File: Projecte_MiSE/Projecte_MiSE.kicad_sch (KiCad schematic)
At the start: 30 parts, among them J1 conn_DFrobot, U1 LMV324

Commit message: components add
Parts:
- removed C?: 100n, Capacitor_SMD:C_0805_2012Metric, symbol Device:C
- removed J?: ESP01_WiFi_mod, Connector_PinSocket_2.54mm:PinSocket_2x04_P2.54mm_Vertical, symbol Connector_Generic:Conn_02x04_Odd_Even
- removed J?: Conn_RX_TP, Connector_PinHeader_2.00mm:PinHeader_1x01_P2.00mm_Vertical, symbol Connector:Conn_01x01_Pin
- removed J?: Conn_TX_TP, Connector_PinHeader_2.00mm:PinHeader_1x01_P2.00mm_Vertical, symbol Connector:Conn_01x01_Pin
- removed J?: Conn_01x03, symbol Connector_Generic:Conn_01x03
- removed J?: Conn_01x05, symbol Connector_Generic:Conn_01x05
- removed R?: R, symbol Device:R
- added C? (x6): C, symbol Device:C
- added C_RXD: C_TXD, symbol Connector:Conn_01x02_Pin
- added J?: Conn_01x03_Pin, symbol Connector:Conn_01x03_Pin
- added J?: ESP01, symbol Connector_Generic:Conn_02x04_Odd_Even
- added J?: URM10, symbol Connector:Conn_01x05_Pin
- added R? (x3): R, symbol Device:R
- J1: value conn_DFrobot -> C_DFrobot
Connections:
- net +3.3V: now also LCD?.1 (VDD), C?.1, C?.1, C?.1, J?.2 (Pin_2), R?.1, R?.1, R?.1; no longer J1.1 (Pin_1), J1.2 (Pin_2)
- net GND: now also LCD?.2 (VSS), LCD?.6 (A), LCD?.7 (K), C?.2, C?.2, C?.2, C?.2, C?.2, C?.2, J?.3 (Pin_3), J?.5 (Pin_5), J?.7 (Pin_7)
- net GPIOD: now also IC?.36 (P3.6/OA3-)
- net GPIOL: now also IC?.44 (P3.3/OA2+)
- net GPIOR: now also IC?.45 (P3.2/OA2-)
- net GPIOU: now also IC?.35 (P3.7/OA3+)
- net JSEL: now also IC?.37 (P3.5/OA3O); no longer IC?.44 (P3.3/OA2+)
- net at IC?.12 (P4.7/UCB1SOMI/UCB1SCL), J1.9 (Pin_9): now also LCD?.4 (SCL), R?.2
- net at IC?.13 (P4.6/UCB1SIMO/UCB1SDA), J1.11 (Pin_11): now also LCD?.3 (SDA), R?.2
- net at IC?.14 (P4.5/UCB1CLK): now also LCD?.5 (RST)
- net EN: now reaches IC?.17 (P6.5/TB3.6)
- net EN: now also J?.6 (Pin_6), R?.2
- net P12: now reaches IC?.18 (P6.4/TB3.5)
- net P12: now also J1.12 (Pin_12)
- net P8: now reaches IC?.19 (P6.3/TB3.4)
- net P8: now also J1.10 (Pin_10)
- net P2: now reaches IC?.20 (P6.2/TB3.3)
- net P2: now also J1.8 (Pin_8)
- net P1: now reaches IC?.21 (P6.1/TB3.2)
- net P1: now also J1.6 (Pin_6)
- net P0: now reaches IC?.22 (P6.0/TB3.1)
- net P0: now also J1.4 (Pin_4)
- net TXD: now reaches IC?.23 (P4.3/UCA1TXD/UCA1SIMO/~{UCA1TXD})
- net TXD: now also C_RXD.1 (Pin_1), J?.8 (Pin_8)
- net RXD: now reaches IC?.24 (P4.2/UCA1RXD/UCA1SOMI/~{UCA1RXD})
- net RXD: now also C_RXD.2 (Pin_2), J?.1 (Pin_1)
- net trg: now reaches IC?.27 (P2.3/TB1TRG)
- net trg: now also J?.3 (Pin_3)
- net at IC?.29 (P2.1/TB1.2/COMP1.O): now also J?.2 (Pin_2)
- net MOSI: now reaches IC?.31 (P1.7/UCA0TXD/UCA0SIMO/TB0.2/TDO/OA1+/A7/VREF+)
- net MOSI: now also J1.7 (Pin_7)
- net MISO: now reaches IC?.32 (P1.6/UCA0RXD/UCA0SOMI/TB0.1/TDI/TCLK/OA1-/A6)
- net MISO: now also J1.5 (Pin_5)
- net SCLK: now reaches IC?.33 (P1.5/UCA0CLK/TMS/OA1O/A5)
- net SCLK: now also J1.3 (Pin_3)
- net at IC?.4 (TEST/SBWTCK): now also J?.2 (Pin_2)
- net at C?.1, IC?.5 (~{RST}/NMI/SBWTDIO), R?.2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: now also J?.1 (Pin_1)
- new net: C?.1, J1.1 (Pin_1)
- new net: C?.1, J?.1 (Pin_1)
- new net: C?.1, J1.2 (Pin_2)
- no-connect marks 14 -> 29
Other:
- moved on the sheet: C?, IC?, J1, LCD?, R1, R2, R?, RV1, RV?, S1, SW?, U1A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

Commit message: LAYOUT_RULES
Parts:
- C1, C10, C11, C2, C3, C4, C5, C6, C7, C8, C9: renamed from C?; footprint (none) -> Capacitor_SMD:C_0805_2012Metric
- C_RXD1: renamed from C_RXD; footprint (none) -> Connector_PinHeader_2.54mm:PinHeader_1x02_P2.54mm_Vertical
- IC1: renamed from IC?; footprint MiSE:QFP50P900X900X160-48N -> Package_QFP:LQFP-48_7x7mm_P0.5mm
- J2: renamed from J?; footprint (none) -> Connector_PinHeader_2.54mm:PinHeader_1x03_P2.54mm_Vertical
- J3: renamed from J?; footprint (none) -> Connector_PinSocket_2.54mm:PinSocket_2x04_P2.54mm_Vertical
- J4: renamed from J?; footprint (none) -> Connector_PinSocket_2.54mm:PinSocket_1x05_P2.54mm_Vertical
- LCD1: renamed from LCD?; footprint MiSE:LCD_2x16_I2C(Midas) -> Connector_PinSocket_2.54mm:PinSocket_2x04_P2.54mm_Vertical
- R1: footprint (none) -> Resistor_SMD:R_0805_2012Metric
- R10, R11, R12, R3, R4, R5, R7, R8, R9: renamed from R?; footprint (none) -> Resistor_SMD:R_0805_2012Metric
- S1: footprint THB001P -> MiSE:THB001P
- U1: footprint (none) -> Package_SO:SOIC-14_3.9x8.7mm_P1.27mm
- Y1: renamed from Y?; footprint (none) -> Crystal:Crystal_DS26_D2.0mm_L6.0mm_Horizontal_1EP_style1
- gave numbers to parts that had none: 3
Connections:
- net SCL: now reaches IC1.12 (P4.7/UCB1SOMI/UCB1SCL), J1.9 (Pin_9), LCD1.4 (SCL), R4.2
- net SDA: now reaches IC1.13 (P4.6/UCB1SIMO/UCB1SDA), J1.11 (Pin_11), LCD1.3 (SDA), R5.2

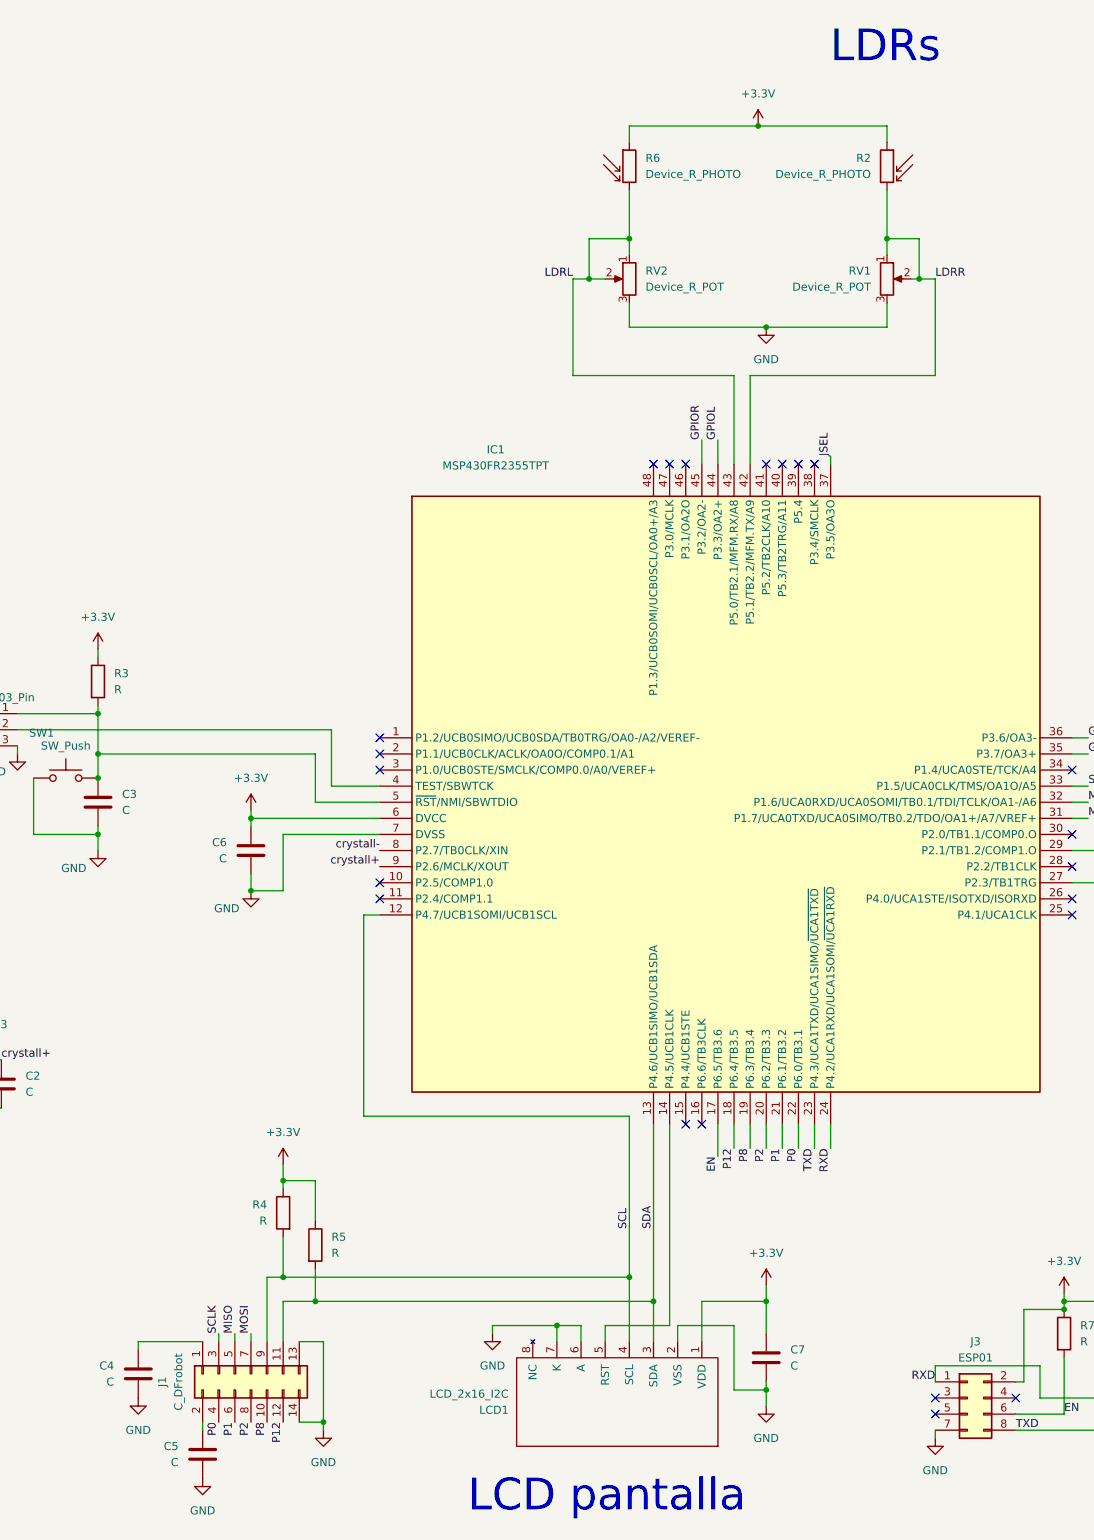
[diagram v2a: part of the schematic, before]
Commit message: layout LCD i DFrobot
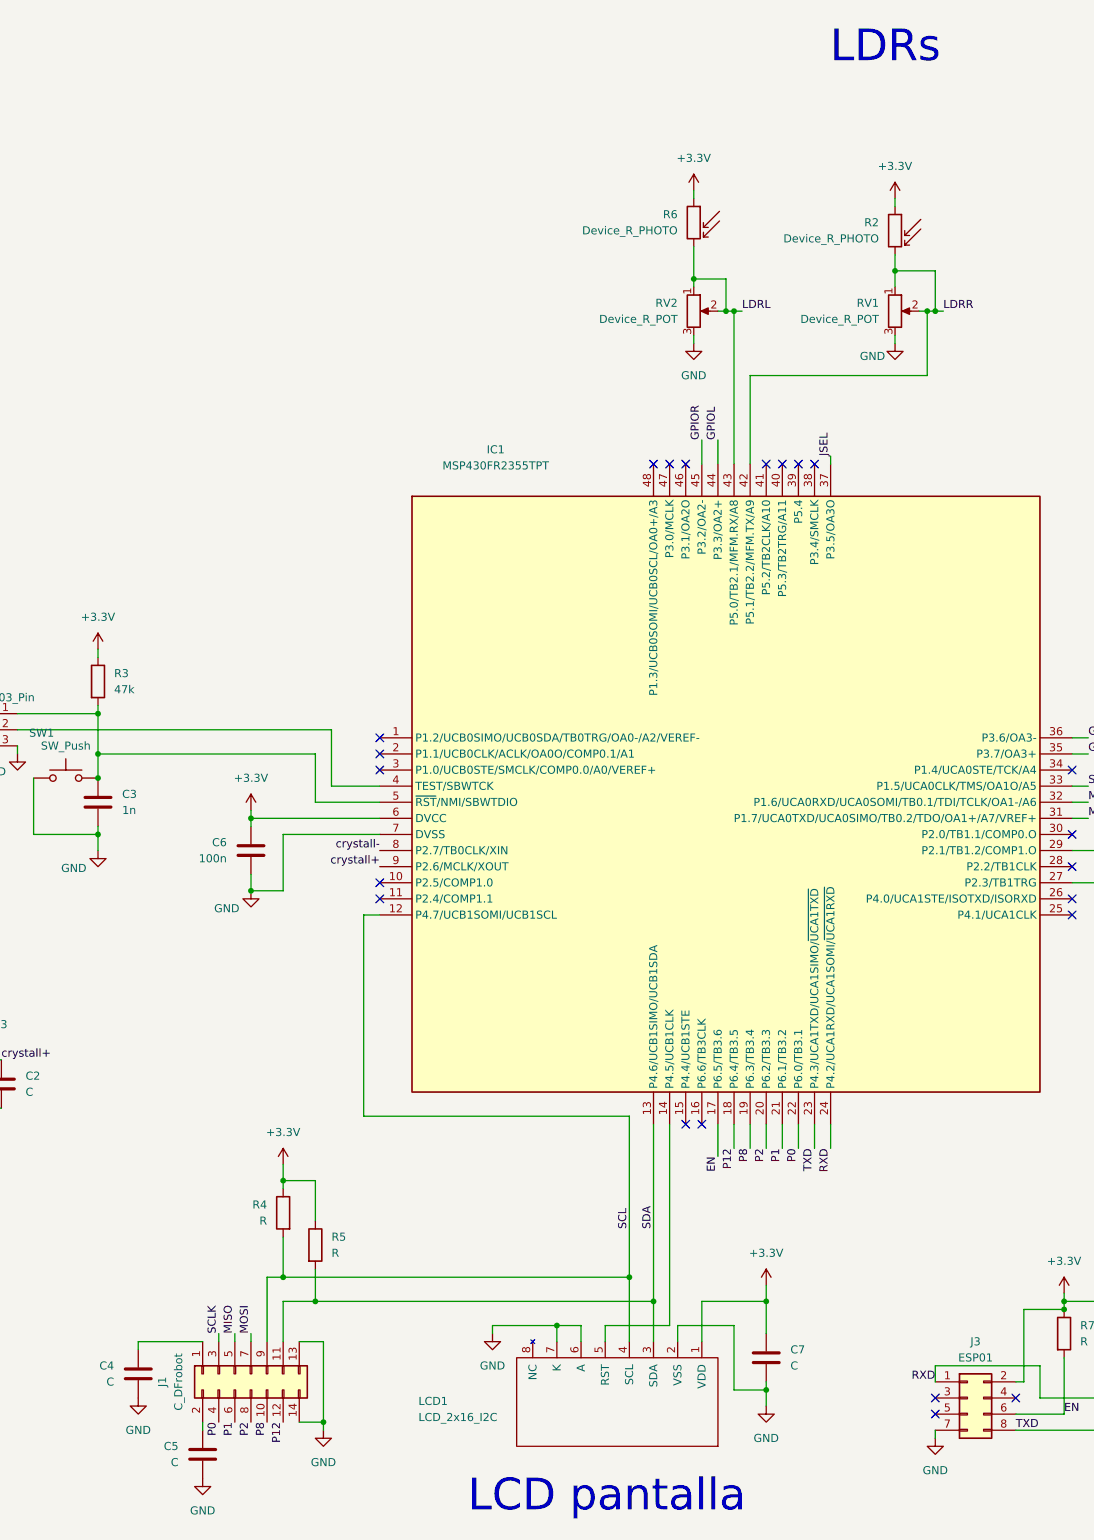
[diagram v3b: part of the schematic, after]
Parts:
- C3: value C -> 1n
- C6: value C -> 100n
- LCD1: footprint Connector_PinSocket_2.54mm:PinSocket_2x04_P2.54mm_Vertical -> MiSE:LCD_2x16_I2C(Midas)
- R3: value R -> 47k
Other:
- moved on the sheet: R2, R6, RV1, RV2

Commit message: test point added
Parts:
- removed C_RXD1: C_TXD, Connector_PinHeader_2.54mm:PinHeader_1x02_P2.54mm_Vertical, symbol Connector:Conn_01x02_Pin
- added D1: LED, LED_SMD:LED_0805_2012Metric, symbol Device:LED
- added J10, J5: Conn_GND_TP, Connector_PinHeader_1.00mm:PinHeader_1x01_P1.00mm_Vertical, symbol Connector:Conn_01x01_Pin
- added J11: Conn_TXD_TP, Connector_PinHeader_1.00mm:PinHeader_1x01_P1.00mm_Vertical, symbol Connector:Conn_01x01_Pin
- added J12: Conn_RXD_TP, Connector_PinHeader_1.00mm:PinHeader_1x01_P1.00mm_Vertical, symbol Connector:Conn_01x01_Pin
- added J6: Conn_ACLK_TP, Connector_PinHeader_1.00mm:PinHeader_1x01_P1.00mm_Vertical, symbol Connector:Conn_01x01_Pin
- added J7: Conn_SMCLK_TP, Connector_PinHeader_1.00mm:PinHeader_1x01_P1.00mm_Vertical, symbol Connector:Conn_01x01_Pin
- added J8: Conn_SDA_TP, Connector_PinHeader_1.00mm:PinHeader_1x01_P1.00mm_Vertical, symbol Connector:Conn_01x01_Pin
- added J9: Conn_SCL_TP, Connector_PinHeader_1.00mm:PinHeader_1x01_P1.00mm_Vertical, symbol Connector:Conn_01x01_Pin
- added R13: R, Resistor_SMD:R_0805_2012Metric, symbol Device:R
- C1, C2: value C -> 15p
- C4, C5, C7, C8, C9: value C -> 100n
- J2: value Conn_01x03_Pin -> Conn_SWB
- J3: value ESP01 -> ESP01_WIFI
- R4, R5: value R -> 2k2
- R7: value R -> 10k
- SW1: value SW_Push -> ~{RST}
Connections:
- net +3.3V: now also C4.1, C5.1, C9.1, J1.1 (Pin_1), J1.2 (Pin_2), J4.1 (Pin_1)
- net EN: now also IC1.15 (P4.4/UCB1STE); no longer IC1.17 (P6.5/TB3.6)
- net GND: now also J10.1 (Pin_1), J5.1 (Pin_1), R13.1
- net RXD: now also J12.1 (Pin_1)
- net SCL: now also J9.1 (Pin_1)
- net SDA: now also J8.1 (Pin_1)
- net TXD: now also J11.1 (Pin_1)
- net SBWTDIO: now reaches C3.1, IC1.5 (~{RST}/NMI/SBWTDIO), J2.1 (Pin_1), R3.2, SW1.2
- net SBWTCK: now reaches IC1.4 (TEST/SBWTCK), J2.2 (Pin_2)
- net THD: now reaches R11.2, R12.1, U1.13 (-)
- net THR: now reaches R1.1, R8.2, U1.3 (+)
- net THL: now reaches R1.2, R9.1, U1.6 (-)
- net ~{RST_{LCD}}: now reaches IC1.14 (P4.5/UCB1CLK), LCD1.5 (RST)
- net ACLK_TP: now reaches IC1.2 (P1.1/UCB0CLK/ACLK/OA0O/COMP0.1/A1)
- net ACLK_TP: now also J6.1 (Pin_1)
- net echo: now reaches IC1.29 (P2.1/TB1.2/COMP1.O), J4.2 (Pin_2)
- net SMCLK_TP: now reaches IC1.3 (P1.0/UCB0STE/SMCLK/COMP0.0/A0/VEREF+)
- net SMCLK_TP: now also J7.1 (Pin_1)
- net THU: now reaches R10.2, R11.1, U1.10 (+)
- new net L_R: D1.1 (K), R13.2
- new net M_L: D1.2 (A), IC1.17 (P6.5/TB3.6)
- no-connect marks 29 -> 26
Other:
- note added: "CONN_ROBOT"
- note added: "LED PWM"
- note added: "Mòdul WIFI"
- note added: "Quars oscil·lador"
- note added: "SBW"
- note added: "Ultrasons"
- moved on the sheet: C1, C2, C4, C5, C8, J1, J3, R2, R4, R5, R6, R7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

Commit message: footprints and layout
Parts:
- J10, J11, J12, J5, J6, J7, J8, J9: footprint Connector_PinHeader_1.00mm:PinHeader_1x01_P1.00mm_Vertical -> Connector_PinHeader_2.54mm:PinHeader_1x01_P2.54mm_Vertical
- J4: footprint Connector_PinSocket_2.54mm:PinSocket_1x05_P2.54mm_Vertical -> Connector_PinHeader_2.54mm:PinHeader_1x05_P2.54mm_Vertical
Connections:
- net M_L: now also IC1.30 (P2.0/TB1.1/COMP0.O); no longer IC1.17 (P6.5/TB3.6)
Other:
- moved on the sheet: D1, R13
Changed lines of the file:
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@@
 	)
 	(rectangle
-		(start 159.385 215.9)
-		(end 186.69 227.33)
+		(start 236.855 124.46)
+		(end 264.16 135.89)
 		(stroke
 			(width 0)
@@
 	)
 	(rectangle
-		(start 226.695 139.7)
-		(end 277.495 190.5)
+		(start 232.41 139.7)
+		(end 283.21 190.5)
 		(stroke
 			(width 0)
@@
 	(text "Ultrasons\n"
 		(exclude_from_sim no)
-		(at 252.222 144.78 0)
+		(at 263.906 145.034 0)
 		(effects
 			(font
@@
 	(text "LED PWM"
 		(exclude_from_sim no)
-		(at 171.45 225.806 0)
+		(at 248.92 134.366 0)
 		(effects
 			(font
@@
 	)
 	(no_connect
-		(at 215.9 163.83)
-	)
-	(no_connect
 		(at 252.73 173.99)
 	)
@@
 	)
 	(no_connect
+		(at 160.02 209.55)
+	)
+	(no_connect
 		(at 210.82 252.73)
 	)
@@
 	(wire
 		(pts
+			(xy 215.9 163.83) (xy 228.6 163.83)
+		)
+		(stroke
+			(width 0)
+			(type default)
+		)
+	)
+	(wire
+		(pts
 			(xy 66.04 247.65) (xy 69.85 247.65)
 		)
@@
 	(wire
 		(pts
+			(xy 228.6 128.27) (xy 237.49 128.27)
+		)
+		(stroke
+			(width 0)
+			(type default)
+		)
+	)
+	(wire
+		(pts
 			(xy 49.53 149.86) (xy 49.53 151.13)
 		)
@@
 	(wire
 		(pts
+			(xy 228.6 163.83) (xy 228.6 128.27)
+		)
+		(stroke
+			(width 0)
+			(type default)
+		)
+	)
+	(wire
+		(pts
 			(xy 187.96 68.58) (xy 187.96 71.12)
 		)
@@
 	(wire
 		(pts
-			(xy 160.02 209.55) (xy 160.02 219.71)
-		)
-		(stroke
-			(width 0)
-			(type default)
-		)
-	)
-	(wire
-		(pts
 			(xy 317.5 91.44) (xy 317.5 99.06)
 		)
@@
 	(wire
 		(pts
-			(xy 177.8 219.71) (xy 182.88 219.71)
+			(xy 255.27 128.27) (xy 260.35 128.27)
 		)
 		(stroke
@@
 	(wire
 		(pts
-			(xy 167.64 219.71) (xy 170.18 219.71)
+			(xy 245.11 128.27) (xy 247.65 128.27)
 		)
 		(stroke
@@
 	(wire
 		(pts
-			(xy 182.88 219.71) (xy 182.88 220.98)
+			(xy 260.35 128.27) (xy 260.35 129.54)
 		)
 		(stroke
@@
 	)
 	(label "M_L"
-		(at 160.02 217.17 180)
+		(at 228.6 130.81 180)
 		(effects
 			(font
@@
 	)
 	(label "echo"
-		(at 233.68 168.91 0)
+		(at 236.22 168.91 0)
 		(effects
 			(font
@@
 	)
 	(label "trg"
-		(at 233.68 171.45 0)
+		(at 236.22 171.45 0)
 		(effects
 			(font
@@
 	)
 	(label "L_R"
-		(at 170.18 219.71 270)
+		(at 247.65 128.27 270)
 		(effects
 			(font
@@
 			)
 		)
-		(property "Footprint" "Connector_PinHeader_1.00mm:PinHeader_1x01_P1.00mm_Vertical"
+		(property "Footprint" "Connector_PinHeader_2.54mm:PinHeader_1x01_P2.54mm_Vertical"
 			(at 128.27 213.36 0)
 			(effects
@@
 	(symbol
 		(lib_id "power:GND")
-		(at 182.88 220.98 0)
+		(at 260.35 129.54 0)
 		(unit 1)
 		(exclude_from_sim no)
@@
 		(fields_autoplaced yes)
 		(property "Reference" "#PWR025"
-			(at 182.88 227.33 0)
+			(at 260.35 135.89 0)
 			(effects
 				(font
@@
 		)
 		(property "Value" "GND"
-			(at 182.88 226.06 0)
+			(at 260.35 134.62 0)
 			(effects
 				(font
@@
 		)
 		(property "Footprint" ""
-			(at 182.88 220.98 0)
+			(at 260.35 129.54 0)
 			(effects
 				(font
@@
 		)
 		(property "Datasheet" ""
-			(at 182.88 220.98 0)
+			(at 260.35 129.54 0)
 			(effects
 				(font
@@
 		)
 		(property "Description" "Power symbol creates a global label with name \"GND\" , ground"
-			(at 182.88 220.98 0)
+			(at 260.35 129.54 0)
 			(effects
 				(font
@@
 			)
 		)
-		(property "Footprint" "Connector_PinHeader_1.00mm:PinHeader_1x01_P1.00mm_Vertical"
+		(property "Footprint" "Connector_PinHeader_2.54mm:PinHeader_1x01_P2.54mm_Vertical"
 			(at 231.14 252.73 0)
 			(effects
@@
 	(symbol
 		(lib_id "Device:R")
-		(at 173.99 219.71 270)
+		(at 251.46 128.27 270)
 		(unit 1)
 		(exclude_from_sim no)
@@
 		(dnp no)
 		(property "Reference" "R13"
-			(at 173.99 216.916 90)
+			(at 251.46 125.476 90)
 			(effects
 				(font
@@
 		)
 		(property "Value" "R"
-			(at 174.244 221.996 90)
+			(at 251.714 130.556 90)
 			(effects
 				(font
@@
 		)
 		(property "Footprint" "Resistor_SMD:R_0805_2012Metric"
-			(at 173.99 217.932 90)
+			(at 251.46 126.492 90)
 			(effects
 				(font
@@
 		)
 		(property "Datasheet" "~"
-			(at 173.99 219.71 0)
+			(at 251.46 128.27 0)
 			(effects
 				(font
@@
 		)
 		(property "Description" "Resistor"
-			(at 173.99 219.71 0)
+			(at 251.46 128.27 0)
 			(effects
 				(font
@@
 			)
 		)
-		(property "Footprint" "Connector_PinHeader_1.00mm:PinHeader_1x01_P1.00mm_Vertical"
+		(property "Footprint" "Connector_PinHeader_2.54mm:PinHeader_1x01_P2.54mm_Vertical"
 			(at 76.2 105.41 0)
 			(effects
@@
 			)
 		)
-		(property "Footprint" "Connector_PinHeader_1.00mm:PinHeader_1x01_P1.00mm_Vertical"
+		(property "Footprint" "Connector_PinHeader_2.54mm:PinHeader_1x01_P2.54mm_Vertical"
 			(at 74.93 111.76 0)
 			(effects
@@
 			)
 		)
-		(property "Footprint" "Connector_PinHeader_1.00mm:PinHeader_1x01_P1.00mm_Vertical"
+		(property "Footprint" "Connector_PinHeader_2.54mm:PinHeader_1x01_P2.54mm_Vertical"
 			(at 128.27 218.44 0)
 			(effects
@@
 			)
 		)
-		(property "Footprint" "Connector_PinHeader_1.00mm:PinHeader_1x01_P1.00mm_Vertical"
+		(property "Footprint" "Connector_PinHeader_2.54mm:PinHeader_1x01_P2.54mm_Vertical"
 			(at 128.27 224.79 0)
 			(effects
@@
 			)
 		)
-		(property "Footprint" "Connector_PinHeader_1.00mm:PinHeader_1x01_P1.00mm_Vertical"
+		(property "Footprint" "Connector_PinHeader_2.54mm:PinHeader_1x01_P2.54mm_Vertical"
 			(at 76.2 100.33 0)
 			(effects
@@
 			)
 		)
-		(property "Footprint" "Connector_PinHeader_1.00mm:PinHeader_1x01_P1.00mm_Vertical"
+		(property "Footprint" "Connector_PinHeader_2.54mm:PinHeader_1x01_P2.54mm_Vertical"
 			(at 229.87 257.81 0)
 			(effects
@@
 	(symbol
 		(lib_id "Device:LED")
-		(at 163.83 219.71 180)
+		(at 241.3 128.27 180)
 		(unit 1)
 		(exclude_from_sim no)
@@
 		(dnp no)
 		(property "Reference" "D1"
-			(at 163.576 222.25 0)
+			(at 241.046 130.81 0)
 			(effects
 				(font
@@
 		)
 		(property "Value" "LED"
-			(at 166.878 222.25 0)
+			(at 244.348 130.81 0)
 			(effects
 				(font
@@
 		)
 		(property "Footprint" "LED_SMD:LED_0805_2012Metric"
-			(at 163.83 219.71 0)
+			(at 241.3 128.27 0)
 			(effects
 				(font
@@
 		)
 		(property "Datasheet" "~"
-			(at 163.83 219.71 0)
+			(at 241.3 128.27 0)
 			(effects
 				(font
@@
 		)
 		(property "Description" "Light emitting diode"
-			(at 163.83 219.71 0)
+			(at 241.3 128.27 0)
 			(effects
 				(font
@@
 			)
 		)
-		(property "Footprint" "Connector_PinSocket_2.54mm:PinSocket_1x05_P2.54mm_Vertical"
+		(property "Footprint" "Connector_PinHeader_2.54mm:PinHeader_1x05_P2.54mm_Vertical"
 			(at 257.81 171.45 0)
 			(effects
